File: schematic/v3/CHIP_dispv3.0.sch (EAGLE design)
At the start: 38 parts, among them J1 2X20-CHIPB, J3 S2B-PH-SM4-TB, Q1 NPN-DTC114YUA, Q2 PNP-DTA114YUA, U1 LMR62421, U3 DS2431P, X1 FH12-40S-0.5SH

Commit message: added v3 incl gerber
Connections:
- net GND: now also X1-23.1, X1-7.1
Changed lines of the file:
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@@
 <wire x1="546.1" y1="177.8" x2="546.1" y2="172.72" width="0.1524" layer="91"/>
 <wire x1="546.1" y1="172.72" x2="546.1" y2="170.18" width="0.1524" layer="91"/>
-<wire x1="546.1" y1="170.18" x2="546.1" y2="165.1" width="0.1524" layer="91"/>
+<wire x1="546.1" y1="170.18" x2="546.1" y2="167.64" width="0.1524" layer="91"/>
 <pinref part="X1" gate="-6" pin="1"/>
+<wire x1="546.1" y1="167.64" x2="546.1" y2="165.1" width="0.1524" layer="91"/>
 <wire x1="571.5" y1="170.18" x2="546.1" y2="170.18" width="0.1524" layer="91"/>
 <junction x="546.1" y="170.18"/>
@@
 <pinref part="X1" gate="-1" pin="1"/>
 <wire x1="571.5" y1="182.88" x2="546.1" y2="182.88" width="0.1524" layer="91"/>
+<pinref part="X1" gate="-7" pin="1"/>
+<wire x1="571.5" y1="167.64" x2="546.1" y2="167.64" width="0.1524" layer="91"/>
+<junction x="546.1" y="167.64"/>
+<label x="556.26" y="167.64" size="1.778" layer="95"/>
 </segment>
 <segment>
@@
 <wire x1="543.56" y1="132.08" x2="543.56" y2="129.54" width="0.1524" layer="91"/>
 <pinref part="X1" gate="-22" pin="1"/>
-<wire x1="543.56" y1="129.54" x2="543.56" y2="121.92" width="0.1524" layer="91"/>
+<wire x1="543.56" y1="129.54" x2="543.56" y2="127" width="0.1524" layer="91"/>
+<wire x1="543.56" y1="127" x2="543.56" y2="121.92" width="0.1524" layer="91"/>
 <wire x1="543.56" y1="121.92" x2="543.56" y2="111.76" width="0.1524" layer="91"/>
 <wire x1="571.5" y1="129.54" x2="543.56" y2="129.54" width="0.1524" layer="91"/>
@@
 <wire x1="538.48" y1="121.92" x2="543.56" y2="121.92" width="0.1524" layer="91"/>
 <junction x="543.56" y="121.92"/>
+<pinref part="X1" gate="-23" pin="1"/>
+<wire x1="571.5" y1="127" x2="543.56" y2="127" width="0.1524" layer="91"/>
+<junction x="543.56" y="127"/>
 </segment>
 <segment>

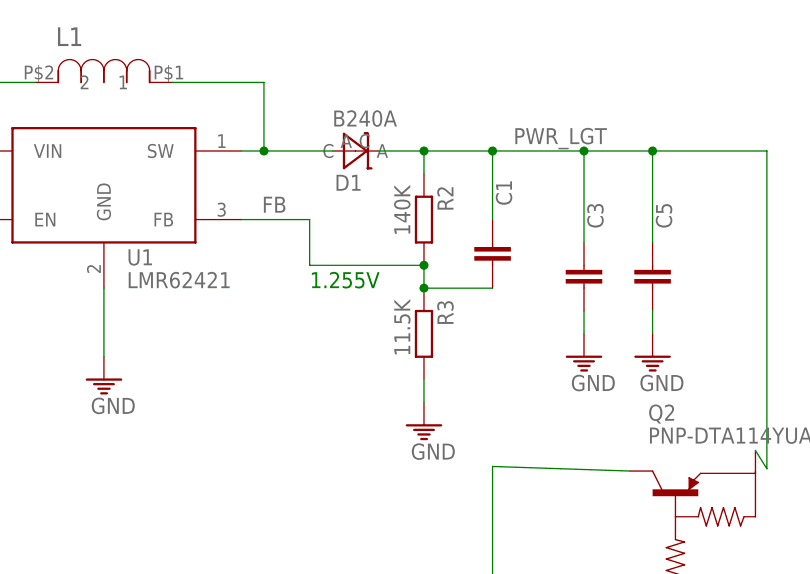
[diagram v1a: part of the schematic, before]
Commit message: recalc resistor to generate 19.2V
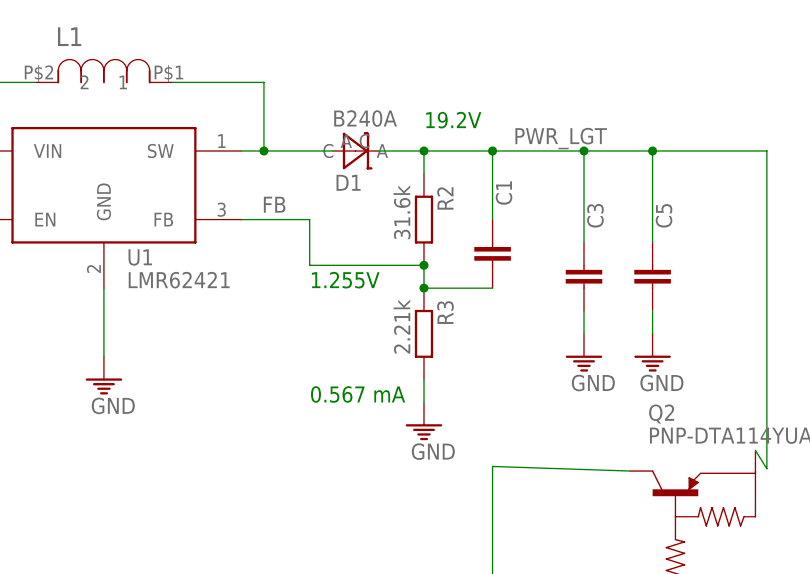
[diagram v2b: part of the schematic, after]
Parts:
- R2: value 140K -> 31.6k
- R3: value 11.5K -> 2.21k
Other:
- note added: "0.567 mA"
- note added: "19.2V"
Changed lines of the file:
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@@
 <part name="U1" library="PocketCHIP-Components-v0.7" deviceset="LMR62421" device=""/>
 <part name="R1" library="rcl" deviceset="R-EU_" device="M0805" value="100K"/>
-<part name="R2" library="rcl" deviceset="R-EU_" device="M0805" value="140K"/>
-<part name="R3" library="rcl" deviceset="R-EU_" device="M0805" value="11.5K"/>
+<part name="R2" library="rcl" deviceset="R-EU_" device="M0805" value="31.6k"/>
+<part name="R3" library="rcl" deviceset="R-EU_" device="M0805" value="2.21k"/>
 <part name="U$8" library="Keyboard v0.2" deviceset="GND" device=""/>
 <part name="U$12" library="Keyboard v0.2" deviceset="GND" device=""/>
@@
 <text x="236.22" y="81.28" size="1.778" layer="94" font="vector" ratio="12">1W EEPROM</text>
 <text x="530.86" y="246.38" size="1.778" layer="91">1.255V</text>
+<text x="543.56" y="264.16" size="1.778" layer="91">19.2V</text>
+<text x="530.86" y="233.68" size="1.778" layer="91">0.567 mA</text>
 </plain>
 <instances>
